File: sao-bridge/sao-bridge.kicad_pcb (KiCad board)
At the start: 2 copper layers, 156.8 x 17.7 mm, 6 parts, among them J1 SAO_LEFT, J2 BADGE_LEFT, J3 SAO_MID, J4 BADGE_RIGHT, J5 SAO_RIGHT, J6 GPIO_MID

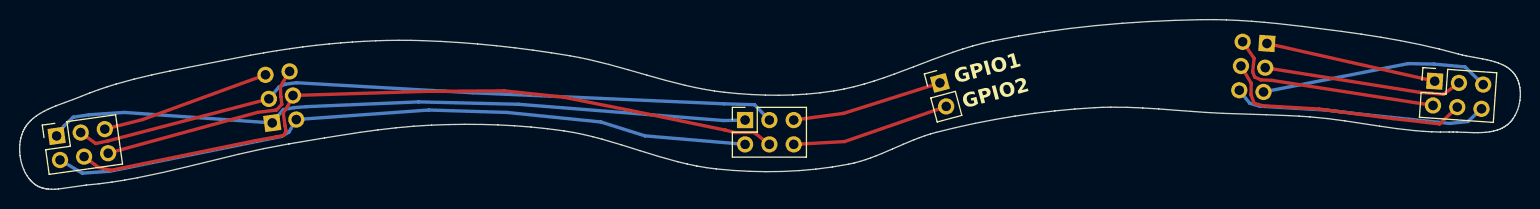
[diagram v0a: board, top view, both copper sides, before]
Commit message: add some info to bottom siklscreen
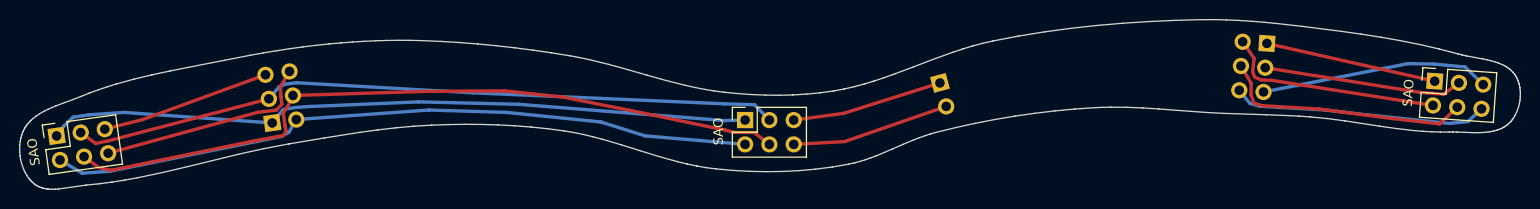
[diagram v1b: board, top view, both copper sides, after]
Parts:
- J6: moved to B.Cu
- turned J6 to -165 degrees
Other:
- board text added: "BADGE"
- board text added: "SAO"
- board text added: "This"
- board text added: "badge"
- board text added: "faces"
- board text added: "github.com/astuder/ supercon8-sao-adapters"
- board text added: "side"
- board text added: "towards"
